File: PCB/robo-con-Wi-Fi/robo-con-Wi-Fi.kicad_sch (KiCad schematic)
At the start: 124 parts, among them J1 Conn_01x04, J2 SMA-J, J3 Conn_01x05, J4 Conn_01x01, J5 Conn_01x02, J6 Conn_01x01, J7 Conn_01x06, Q1 2SC3325-Y, SW1 SW_Push, SW2 SW_Push, U1 STM32H723VGTx, U10 MCP73831-2-OT, U11 LM66100DCK, U12 NJM12877, U13 TXB0606DYYR, U14 TPS628513DRLR, U15 LM66100DCK, U18 USB_Type-C, U2 LBEE5HY2FY, U3 TXU0204, U5 RKJXV122400R, U6 IS25LP064D-JLLE, U7 RKJXV122400R, U8 TMHU28, U9 TMHU28, Y2 XRCGB25M000FFS1AR0

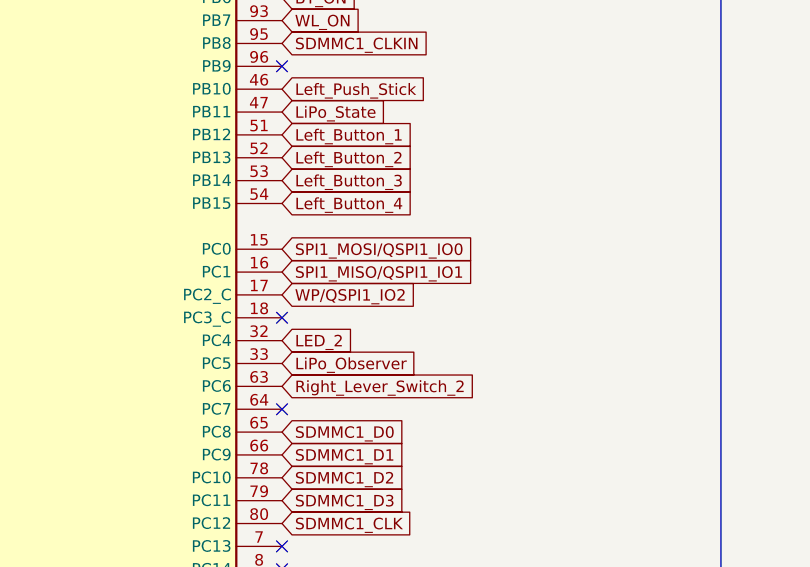
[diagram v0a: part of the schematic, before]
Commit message: ピンの位置ずれ
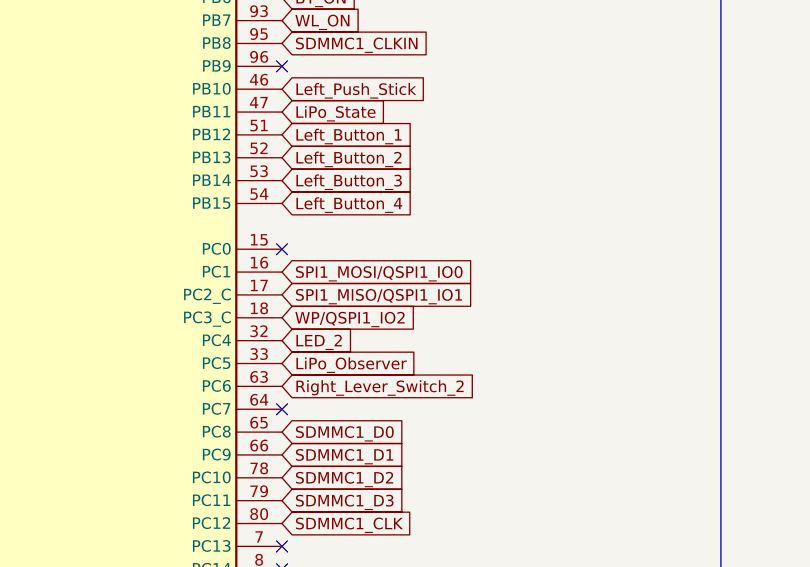
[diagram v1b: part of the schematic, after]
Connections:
- net SPI1_MISO/QSPI1_IO1: now also U1.17 (PC2_C); no longer U1.16 (PC1)
- net SPI1_MOSI/QSPI1_IO0: now also U1.16 (PC1); no longer U1.15 (PC0)
- net WP/QSPI1_IO2: now also U1.18 (PC3_C); no longer U1.17 (PC2_C)
